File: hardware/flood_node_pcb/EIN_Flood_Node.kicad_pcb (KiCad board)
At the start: 4 copper layers, 100 x 80 mm, 19 parts, among them U1 ESP32-S3, U2 SX1276_LoRa, U3 SHT31, U4 DS3231_RTC, U5 ADS1115, U6 BQ24650_MPPT

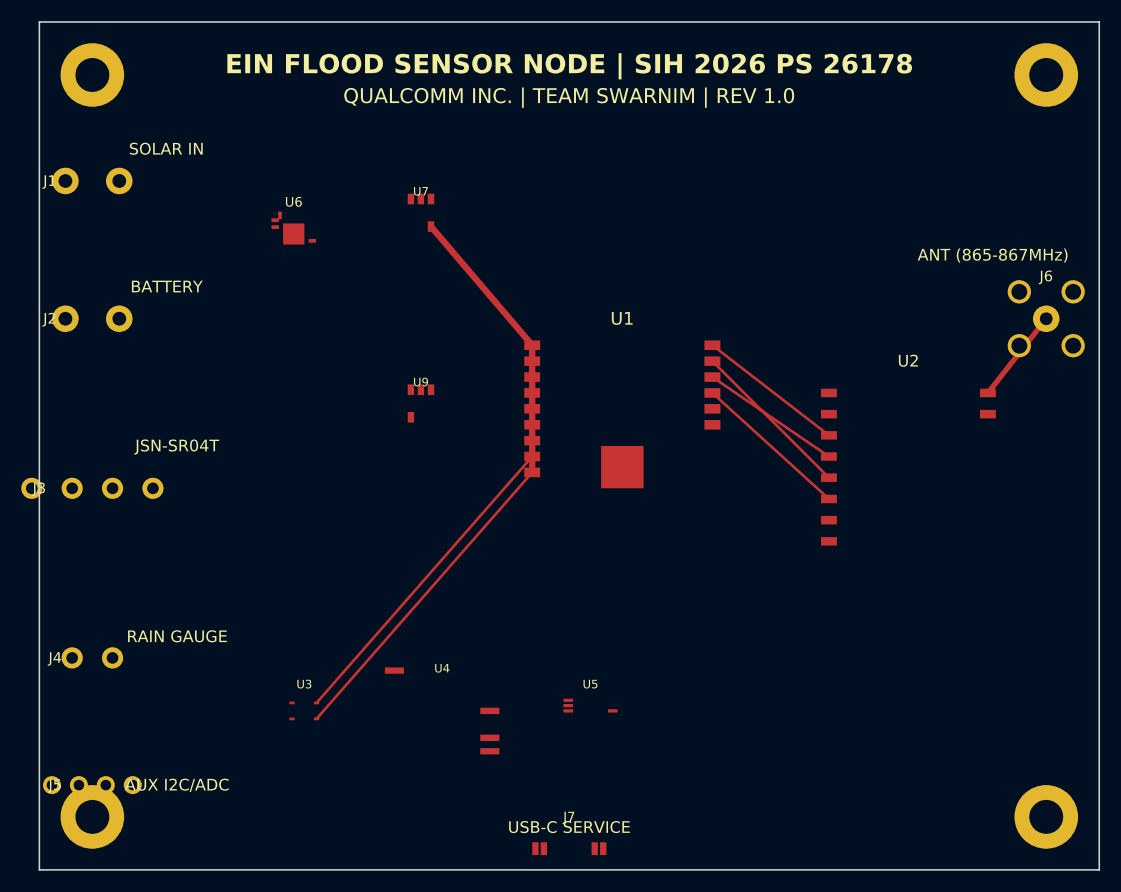
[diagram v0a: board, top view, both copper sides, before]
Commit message: Fix KiCanvas white screen: remove unsupported comments in PCB and align schematic syntax
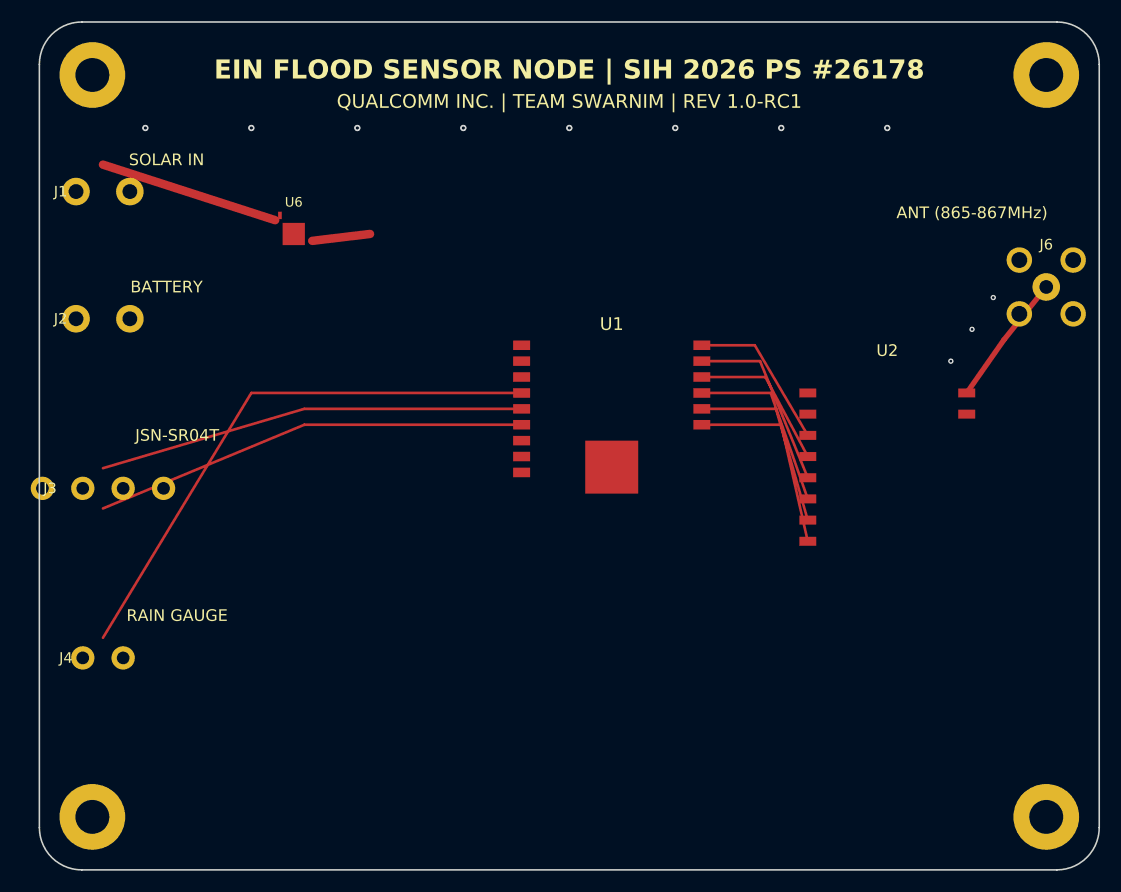
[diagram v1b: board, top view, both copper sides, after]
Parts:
- removed J5: , Connector_PinHeader_2.54mm:PinHeader_1x04_P2.54mm_Vertical
- removed J7: , Connector_USB:USB_C_Receptacle_HRO_TYPE-C-31-M-12
- removed U3: SHT31, Package_DFN_QFN:DFN-8-1EP_2.5x2.5mm_P0.5mm_EP1.4x1.7mm
- removed U4: DS3231_RTC, Package_SO:SOIC-16W_7.5x10.3mm_P1.27mm
- removed U5: ADS1115, Package_SO:MSOP-10_3x3mm_P0.5mm
- removed U7: , Package_TO_SOT_SMD:SOT-23-5
- removed U9: , Package_TO_SOT_SMD:SOT-23-6
- U1: value ESP32-S3 -> (none)
- U2: value SX1276_LoRa -> (none)
- U6: value BQ24650_MPPT -> (none)
- moved J6 3.00 mm to (95.0, 25.0)
- moved U2 2.00 mm to (80.0, 42.0)
- moved J1 1.41 mm to (6.00, 16.0)
- moved J2 1.00 mm to (6.00, 28.0)
- moved J3 1.00 mm to (6.00, 44.0)
- moved J4 1.00 mm to (6.00, 60.0)
- moved U1 1.00 mm to (54.0, 42.0)
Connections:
- net VBAT_LIFEPO4 renamed VBAT
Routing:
- net RAIN_IRQ: track 0.00 -> 52.5 mm
- net JSN_ECHO_DIV: track 0.00 -> 41.1 mm
- net JSN_TRIG: track 0.00 -> 40.3 mm
- net I2C_SDA: track 30.9 -> 0.00 mm
- net I2C_SCL: track 30.9 -> 0.00 mm
- net +3.3V: track 26.2 -> 0.00 mm
- net LORA_DIO0: track 0.00 -> 18.8 mm
- net LORA_RST: track 0.00 -> 17.9 mm
- net SOLAR_VIN: track 0.00 -> 17.1 mm
- net VBAT: track 0.00 -> 5.49 mm
- net RF_ANT_50R: track 8.90 -> 12.5 mm
- net SPI_MISO: track 14.9 -> 17.1 mm
- net SPI_MOSI: track 15.6 -> 17.4 mm
- net SPI_SCK: track 13.3 -> 14.5 mm
- net LORA_NSS: track 13.9 -> 14.9 mm
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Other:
- outline, holes or cut-outs redrawn
- board text added: "EIN FLOOD SENSOR NODE | SIH 2026 PS #26178"
- board text added: "QUALCOMM INC. | TEAM SWARNIM | REV 1.0-RC1"
- board text removed: "AUX I2C/ADC"
- board text removed: "EIN FLOOD SENSOR NODE | SIH 2026 PS 26178"
- board text removed: "QUALCOMM INC. | TEAM SWARNIM | REV 1.0"
- board text removed: "USB-C SERVICE"

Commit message: adding some research paper
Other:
- board text added: "SWARNIM FLOOD SENSOR NODE | SIH 2026 PS #26178"
- board text removed: "EIN FLOOD SENSOR NODE | SIH 2026 PS #26178"
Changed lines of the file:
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@@
   (paper "A4")
   (title_block
-    (title "EIN Flagship Flood / Water-Level Node - 4-Layer PCB")
-    (date "2026-09-05")
+    (title "SWARNIM Flagship Flood / Water-Level Node - 4-Layer PCB")
+    (date "2026-09-09")
     (rev "v1.0-RC1")
     (company "Team Swarnim | SIH 2026 Problem Statement 26178 (Qualcomm Inc.)")
-    (comment 1 "Dual-Tier Edge AI & LoRa Sensor Node | Board Size: 100mm x 80mm")
+    (comment 1 "Tier 1 Low-Cost Sensor Node | Board Size: 100mm x 80mm")
     (comment 2 "Stackup: L1:Signal/RF | L2:GND | L3:PWR(3V3/5V) | L4:Signal/GND")
   )
@@
     (pad "1" thru_hole circle (at 0 0) (size 6.2 6.2) (drill 3.2) (layers *.Cu *.Mask) (net 1 "GND"))
   )
-  (gr_text "EIN FLOOD SENSOR NODE | SIH 2026 PS #26178" (at 50 4.5) (layer "F.SilkS")
+  (gr_text "SWARNIM FLOOD SENSOR NODE | SIH 2026 PS #26178" (at 50 4.5) (layer "F.SilkS")
     (effects (font (size 1.8 1.8) (thickness 0.32) bold))
   )
